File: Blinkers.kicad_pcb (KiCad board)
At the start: 2 copper layers, 238 x 45 mm, 218 parts, among them J1 12V, J2 A1, J3 gnd, J4 A1, J5 A1, J6 A1, J7 A1, J8 A1, Q1 Q_NMOS_DGS, Q2 Q_NMOS_DGS, Q3 Q_NMOS_DGS, Q4 Q_NMOS_DGS, Q5 Q_NMOS_DGS, Q6 Q_NMOS_DGS

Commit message: Modified D_2835 to make it work with specifications for LEDs. Moved VDD and GND pins to appropriate locations near center of board.
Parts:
- D1, D10, D101, D102, D103, D104, D105, D106, D107, D108, D11, D110, D111, D112, D113, D114, D115, D116, D117, D118, D12, D120, D121, D122, D123, D124, D125, D126, D128, D129, D13, D130, D131, D132, D133, D134, D135, D137, D138, D139, D140, D141, D142, D143, D144, D145, D147, D148, D149, D15, D150, D151, D152, D153, D155, D156, D157, D158, D159, D16, D160, D161, D162, D164, D165, D166, D167, D168, D169, D17, D170, D171, D172, D174, D18, D19, D2, D20, D22, D24, D25, D27, D28, D29, D3, D30, D31, D32, D33, D34, D35, D36, D37, D38, D39, D4, D41, D42, D43, D44, D45, D46, D47, D48, D49, D5, D51, D52, D53, D54, D55, D56, D57, D58, D59, D6, D61, D62, D63, D64, D65, D66, D68, D69, D70, D71, D72, D73, D74, D75, D77, D78, D79, D8, D80, D81, D82, D83, D84, D85, D87, D88, D9, D90, D91, D93, D94, D95, D96, D97, D98, D99: footprint Footprints:D_2835_FLIPPED -> Footprints:D_2835
- moved J3 56.8 mm to (214.6, 119.4)
- moved J1 55.7 mm to (214.6, 104.1)

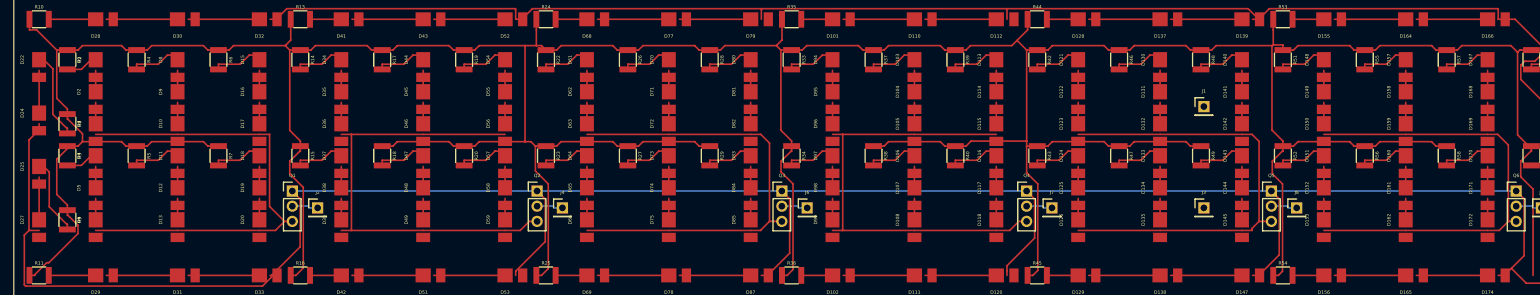
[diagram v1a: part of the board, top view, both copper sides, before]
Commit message: Changed positioning of LED grid with Array tool.
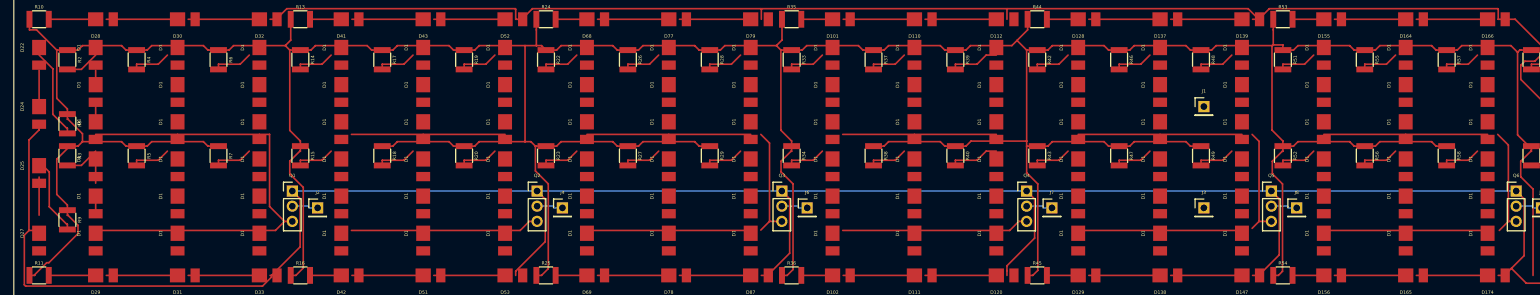
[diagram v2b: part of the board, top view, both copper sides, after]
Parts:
- removed D10, D103, D104, D105, D106, D107, D108, D11, D113, D114, D115, D116, D117, D118, D12, D121, D122, D123, D124, D125, D126, D13, D130, D131, D132, D133, D134, D135, D140, D141, D142, D143, D144, D145, D148, D149, D15, D150, D151, D152, D153, D157, D158, D159, D16, D160, D161, D162, D167, D168, D169, D17, D170, D171, D172, D18, D19, D2, D20, D3, D34, D35, D36, D37, D38, D39, D4, D44, D45, D46, D47, D48, D49, D5, D54, D55, D56, D57, D58, D59, D6, D61, D62, D63, D64, D65, D66, D70, D71, D72, D73, D74, D75, D8, D80, D81, D82, D83, D84, D85, D9, D94, D95, D96, D97, D98, D99: LED, Footprints:D_2835
- added D1: LED, Footprints:D_2835, F.Cu at (257.3, 123.2)
- added D1: LED, Footprints:D_2835, F.Cu at (146.4, 123.2)
- added D1: LED, Footprints:D_2835, F.Cu at (146.4, 95.2)
- added D1: LED, Footprints:D_2835, F.Cu at (134.1, 95.2)
- added D1: LED, Footprints:D_2835, F.Cu at (121.8, 95.2)
- added D1: LED, Footprints:D_2835, F.Cu at (109.5, 95.2)
- added D1: LED, Footprints:D_2835, F.Cu at (97.2, 95.2)
- added D1: LED, Footprints:D_2835, F.Cu at (84.8, 95.2)
- added D1: LED, Footprints:D_2835, F.Cu at (72.5, 95.2)
- added D1: LED, Footprints:D_2835, F.Cu at (60.2, 95.2)
- added D1: LED, Footprints:D_2835, F.Cu at (134.1, 123.2)
- added D1: LED, Footprints:D_2835, F.Cu at (121.8, 123.2)
- added D1: LED, Footprints:D_2835, F.Cu at (109.5, 123.2)
- added D1: LED, Footprints:D_2835, F.Cu at (97.2, 123.2)
- added D1: LED, Footprints:D_2835, F.Cu at (84.8, 123.2)
- added D1: LED, Footprints:D_2835, F.Cu at (72.5, 123.2)
- added D1: LED, Footprints:D_2835, F.Cu at (60.2, 123.2)
- added D1: LED, Footprints:D_2835, F.Cu at (47.9, 123.2)
- added D1: LED, Footprints:D_2835, F.Cu at (257.3, 117.6)
- added D1: LED, Footprints:D_2835, F.Cu at (245.0, 123.2)
- added D1: LED, Footprints:D_2835, F.Cu at (245.0, 117.6)
- added D1: LED, Footprints:D_2835, F.Cu at (232.7, 117.6)
- added D1: LED, Footprints:D_2835, F.Cu at (220.4, 117.6)
- added D1: LED, Footprints:D_2835, F.Cu at (208.0, 117.6)
- added D1: LED, Footprints:D_2835, F.Cu at (195.7, 117.6)
- added D1: LED, Footprints:D_2835, F.Cu at (183.4, 117.6)
- added D1: LED, Footprints:D_2835, F.Cu at (171.1, 117.6)
- added D1: LED, Footprints:D_2835, F.Cu at (158.8, 117.6)
- added D1: LED, Footprints:D_2835, F.Cu at (146.4, 117.6)
- added D1: LED, Footprints:D_2835, F.Cu at (134.1, 117.6)
- added D1: LED, Footprints:D_2835, F.Cu at (232.7, 123.2)
- added D1: LED, Footprints:D_2835, F.Cu at (121.8, 117.6)
- added D1: LED, Footprints:D_2835, F.Cu at (109.5, 117.6)
- added D1: LED, Footprints:D_2835, F.Cu at (97.2, 117.6)
- added D1: LED, Footprints:D_2835, F.Cu at (84.8, 117.6)
- added D1: LED, Footprints:D_2835, F.Cu at (72.5, 117.6)
- added D1: LED, Footprints:D_2835, F.Cu at (60.2, 117.6)
- added D1: LED, Footprints:D_2835, F.Cu at (47.9, 117.6)
- added D1: LED, Footprints:D_2835, F.Cu at (257.3, 112.0)
- added D1: LED, Footprints:D_2835, F.Cu at (245.0, 112.0)
- added D1: LED, Footprints:D_2835, F.Cu at (232.7, 112.0)
- added D1: LED, Footprints:D_2835, F.Cu at (220.4, 123.2)
- added D1: LED, Footprints:D_2835, F.Cu at (220.4, 112.0)
- added D1: LED, Footprints:D_2835, F.Cu at (208.0, 112.0)
- added D1: LED, Footprints:D_2835, F.Cu at (195.7, 112.0)
- added D1: LED, Footprints:D_2835, F.Cu at (183.4, 112.0)
- added D1: LED, Footprints:D_2835, F.Cu at (171.1, 112.0)
- added D1: LED, Footprints:D_2835, F.Cu at (158.8, 112.0)
- added D1: LED, Footprints:D_2835, F.Cu at (146.4, 112.0)
- added D1: LED, Footprints:D_2835, F.Cu at (134.1, 112.0)
- added D1: LED, Footprints:D_2835, F.Cu at (121.8, 112.0)
- added D1: LED, Footprints:D_2835, F.Cu at (109.5, 112.0)
- added D1: LED, Footprints:D_2835, F.Cu at (208.0, 123.2)
- added D1: LED, Footprints:D_2835, F.Cu at (97.2, 112.0)
- added D1: LED, Footprints:D_2835, F.Cu at (84.8, 112.0)
- added D1: LED, Footprints:D_2835, F.Cu at (72.5, 112.0)
- added D1: LED, Footprints:D_2835, F.Cu at (60.2, 112.0)
- added D1: LED, Footprints:D_2835, F.Cu at (47.9, 112.0)
- added D1: LED, Footprints:D_2835, F.Cu at (257.3, 106.4)
- added D1: LED, Footprints:D_2835, F.Cu at (245.0, 106.4)
- added D1: LED, Footprints:D_2835, F.Cu at (232.7, 106.4)
- added D1: LED, Footprints:D_2835, F.Cu at (220.4, 106.4)
- added D1: LED, Footprints:D_2835, F.Cu at (208.0, 106.4)
- added D1: LED, Footprints:D_2835, F.Cu at (195.7, 123.2)
- added D1: LED, Footprints:D_2835, F.Cu at (195.7, 106.4)
- added D1: LED, Footprints:D_2835, F.Cu at (183.4, 106.4)
- added D1: LED, Footprints:D_2835, F.Cu at (171.1, 106.4)
- added D1: LED, Footprints:D_2835, F.Cu at (158.8, 106.4)
- added D1: LED, Footprints:D_2835, F.Cu at (146.4, 106.4)
- added D1: LED, Footprints:D_2835, F.Cu at (134.1, 106.4)
- added D1: LED, Footprints:D_2835, F.Cu at (121.8, 106.4)
- added D1: LED, Footprints:D_2835, F.Cu at (109.5, 106.4)
- added D1: LED, Footprints:D_2835, F.Cu at (97.2, 106.4)
- added D1: LED, Footprints:D_2835, F.Cu at (84.8, 106.4)
- added D1: LED, Footprints:D_2835, F.Cu at (183.4, 123.2)
- added D1: LED, Footprints:D_2835, F.Cu at (72.5, 106.4)
- added D1: LED, Footprints:D_2835, F.Cu at (60.2, 106.4)
- added D1: LED, Footprints:D_2835, F.Cu at (47.9, 106.4)
- added D1: LED, Footprints:D_2835, F.Cu at (257.3, 100.8)
- added D1: LED, Footprints:D_2835, F.Cu at (245.0, 100.8)
- added D1: LED, Footprints:D_2835, F.Cu at (232.7, 100.8)
- added D1: LED, Footprints:D_2835, F.Cu at (220.4, 100.8)
- added D1: LED, Footprints:D_2835, F.Cu at (208.0, 100.8)
- added D1: LED, Footprints:D_2835, F.Cu at (195.7, 100.8)
- added D1: LED, Footprints:D_2835, F.Cu at (183.4, 100.8)
- added D1: LED, Footprints:D_2835, F.Cu at (171.1, 123.2)
- added D1: LED, Footprints:D_2835, F.Cu at (171.1, 100.8)
- added D1: LED, Footprints:D_2835, F.Cu at (158.8, 100.8)
- added D1: LED, Footprints:D_2835, F.Cu at (146.4, 100.8)
- added D1: LED, Footprints:D_2835, F.Cu at (134.1, 100.8)
- added D1: LED, Footprints:D_2835, F.Cu at (121.8, 100.8)
- added D1: LED, Footprints:D_2835, F.Cu at (109.5, 100.8)
- added D1: LED, Footprints:D_2835, F.Cu at (97.2, 100.8)
- added D1: LED, Footprints:D_2835, F.Cu at (84.8, 100.8)
- added D1: LED, Footprints:D_2835, F.Cu at (72.5, 100.8)
- added D1: LED, Footprints:D_2835, F.Cu at (60.2, 100.8)
- added D1: LED, Footprints:D_2835, F.Cu at (158.8, 123.2)
- added D1: LED, Footprints:D_2835, F.Cu at (47.9, 100.8)
- added D1: LED, Footprints:D_2835, F.Cu at (257.3, 95.2)
- added D1: LED, Footprints:D_2835, F.Cu at (245.0, 95.2)
- added D1: LED, Footprints:D_2835, F.Cu at (232.7, 95.2)
- added D1: LED, Footprints:D_2835, F.Cu at (220.4, 95.2)
- added D1: LED, Footprints:D_2835, F.Cu at (208.0, 95.2)
- added D1: LED, Footprints:D_2835, F.Cu at (195.7, 95.2)
- added D1: LED, Footprints:D_2835, F.Cu at (183.4, 95.2)
- added D1: LED, Footprints:D_2835, F.Cu at (171.1, 95.2)
- added D1: LED, Footprints:D_2835, F.Cu at (158.8, 95.2)
- moved D27 2.03 mm to (39.4, 123.2)
- moved D1 1.84 mm to (47.9, 95.2)
- moved D22 1.84 mm to (39.4, 95.2)
- moved D24 0.98 mm to (39.4, 104.1)
- moved D25 0.12 mm to (39.4, 113.0)
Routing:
- net Net-(D1-Pad1): track 2.52 -> 81.5 mm
- net Net-(D123-Pad1): track 69.5 -> 41.5 mm
- net Net-(D150-Pad1): track 69.4 -> 41.5 mm
- net Net-(D63-Pad1): track 69.7 -> 42.0 mm
- net Net-(D105-Pad1): track 68.9 -> 51.4 mm
- net Net-(D36-Pad1): track 69.1 -> 51.6 mm
- net GND: track 597.7 -> 603.4 mm
- net Net-(D22-Pad1): track 5.73 -> 0.00 mm
- net Net-(D25-Pad2): track 12.0 -> 17.7 mm
- net Net-(D25-Pad1): track 5.73 -> 0.00 mm
- net Net-(D65-Pad1): track 2.52 -> 0.00 mm
- net Net-(D97-Pad1): track 2.52 -> 0.00 mm
- net Net-(D94-Pad1): track 2.52 -> 0.00 mm
- net Net-(D98-Pad1): track 2.52 -> 0.00 mm
- net Net-(D83-Pad1): track 2.52 -> 0.00 mm
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
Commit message: Aligned right side of outer ring.
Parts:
- moved D93 2.03 mm to (270.5, 123.2)
- moved D88 1.84 mm to (270.5, 95.2)
- moved D25 0.85 mm to (39.4, 113.9)
- moved D90 0.55 mm to (270.5, 104.6)
- moved D24 0.43 mm to (39.4, 104.6)
- moved D91 0.17 mm to (270.5, 113.3)
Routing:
- net GND: track 603.4 -> 609.1 mm
- net Net-(D88-Pad1): track 5.73 -> 0.00 mm
- net Net-(D91-Pad2): track 6.82 -> 12.5 mm
- net Net-(D91-Pad1): track 5.73 -> 0.00 mm
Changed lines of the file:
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@@
-(kicad_pcb (version 20171130) (host pcbnew "(5.1.2)-2")
+(kicad_pcb (version 20171130) (host pcbnew 5.1.2-f72e74a~84~ubuntu18.04.1)
   (general
     (thickness 1.6)
@@
   )
   (module Footprints:D_2835 locked placed (layer F.Cu)
-    (at 39.37 104.14 270)
+    (at 39.37 104.567 270)
     (fp_text reference D24 (at 0 2.54 270) (layer F.SilkS)
       (effects (font (size 0.5 0.5) (thickness 0.0625)))
@@
   )
   (module Footprints:D_2835 locked placed (layer F.Cu)
-    (at 39.37 113.03 270)
+    (at 39.37 113.883 270)
     (fp_text reference D25 (at 0 2.54 270) (layer F.SilkS)
       (effects (font (size 0.5 0.5) (thickness 0.0625)))
@@
   )
   (module Footprints:D_2835 placed (layer F.Cu)
-    (at 270.51 97.0875 270)
+    (at 270.51 95.25 270)
     (fp_text reference D88 (at 0 2.54 270) (layer F.SilkS)
       (effects (font (size 0.5 0.5) (thickness 0.0625)))
@@
   )
   (module Footprints:D_2835 placed (layer F.Cu)
-    (at 270.51 105.117 270)
+    (at 270.51 104.567 270)
     (fp_text reference D90 (at 0 2.54 270) (layer F.SilkS)
       (effects (font (size 0.5 0.5) (thickness 0.0625)))
@@
   )
   (module Footprints:D_2835 placed (layer F.Cu)
-    (at 270.51 113.146 270)
+    (at 270.51 113.3167 270)
     (fp_text reference D91 (at 0 2.54 270) (layer F.SilkS)
       (effects (font (size 0.5 0.5) (thickness 0.0625)))
@@
   )
   (module Footprints:D_2835 placed (layer F.Cu)
-    (at 270.51 121.175 270)
+    (at 270.51 123.2 270)
     (fp_text reference D93 (at 0 2.54 270) (layer F.SilkS)
       (effects (font (size 0.5 0.5) (thickness 0.0625)))
@@
   (gr_line (start 35.56 87.63) (end 35.56 132.63) (angle 90) (layer Edge.Cuts) (width 0.15))
   (segment (start 47.88 98.6875) (end 47.88 101.205) (width 0.25) (layer F.Cu) (net 1))
+  (segment (start 47.88 103.505) (end 47.88 106.022) (width 0.25) (layer F.Cu) (net 1))
+  (segment (start 47.88 117.958) (end 47.88 120.475) (width 0.25) (layer F.Cu) (net 1))
+  (segment (start 134.12 122.775) (end 121.8 122.775) (width 0.25) (layer F.Cu) (net 1))
+  (segment (start 146.44 122.775) (end 134.12 122.775) (width 0.25) (layer F.Cu) (net 1))
+  (segment (start 208.04 122.775) (end 195.72 122.775) (width 0.25) (layer F.Cu) (net 1))
+  (segment (start 220.36 122.775) (end 208.04 122.775) (width 0.25) (layer F.Cu) (net 1))
+  (segment (start 245 122.775) (end 232.68 122.775) (width 0.25) (layer F.Cu) (net 1))
+  (segment (start 257.32 122.775) (end 245 122.775) (width 0.25) (layer F.Cu) (net 1))
   (segment (start 47.88 96.3875) (end 45.73 98.5375) (width 0.25) (layer F.Cu) (net 2))
   (segment (start 45.73 98.5375) (end 43.625 98.5375) (width 0.25) (layer F.Cu) (net 2))
-  (segment (start 47.88 103.505) (end 47.88 106.022) (width 0.25) (layer F.Cu) (net 1))
+  (segment (start 47.88 113.14) (end 47.88 115.658) (width 0.25) (layer F.Cu) (net 2))
   (segment (start 72.52 108.322) (end 74.0453 108.322) (width 0.25) (layer F.Cu) (net 3))
   (segment (start 74.0453 108.322) (end 74.0453 119.1626) (width 0.25) (layer F.Cu) (net 3))
@@
   (segment (start 60.2 122.775) (end 72.52 122.775) (width 0.25) (layer F.Cu) (net 3))
   (segment (start 47.88 122.775) (end 60.2 122.775) (width 0.25) (layer F.Cu) (net 3))
-  (segment (start 47.88 113.14) (end 47.88 115.658) (width 0.25) (layer F.Cu) (net 2))
   (segment (start 47.88 110.84) (end 45.73 112.99) (width 0.25) (layer F.Cu) (net 4))
   (segment (start 45.73 112.99) (end 43.625 112.99) (width 0.25) (layer F.Cu) (net 4))
-  (segment (start 47.88 117.958) (end 47.88 120.475) (width 0.25) (layer F.Cu) (net 1))
   (segment (start 54.04 98.5375) (end 54.04 97.7622) (width 0.25) (layer F.Cu) (net 5))
   (segment (start 58.6747 96.3875) (end 57.3 97.7622) (width 0.25) (layer F.Cu) (net 5))
@@
   (segment (start 111.08 129.54) (end 111.08 128.9075) (width 0.25) (layer F.Cu) (net 9))
   (segment (start 270.51 106.717) (end 268.9847 106.717) (width 0.25) (layer F.Cu) (net 9))
+  (segment (start 39.37 104.417) (end 39.37 98.6875) (width 0.25) (layer F.Cu) (net 9))
   (segment (start 177.24 110.09) (end 178.8353 110.09) (width 0.25) (layer F.Cu) (net 10))
   (segment (start 187.9647 109.331) (end 179.5943 109.331) (width 0.25) (layer F.Cu) (net 10))
@@
   (segment (start 77.47 119.126) (end 79.8507 119.126) (width 0.25) (layer B.Cu) (net 11))
   (segment (start 79.8507 119.126) (end 80.1047 119.38) (width 0.25) (layer B.Cu) (net 11))
-  (segment (start 39.37 104.417) (end 39.37 98.6875) (width 0.25) (layer F.Cu) (net 9))
   (segment (start 43.625 108.172) (end 43.625 107.3967) (width 0.25) (layer F.Cu) (net 13))
   (segment (start 39.37 96.3875) (end 41.4381 98.4556) (width 0.25) (layer F.Cu) (net 13))
@@
   (segment (start 134.12 108.322) (end 121.8 108.322) (width 0.25) (layer F.Cu) (net 36))
   (segment (start 146.44 108.322) (end 134.12 108.322) (width 0.25) (layer F.Cu) (net 36))
-  (segment (start 134.12 122.775) (end 121.8 122.775) (width 0.25) (layer F.Cu) (net 1))
-  (segment (start 146.44 122.775) (end 134.12 122.775) (width 0.25) (layer F.Cu) (net 1))
   (segment (start 151.13 121.412) (end 149.9547 121.412) (width 0.25) (layer F.Cu) (net 36))
   (segment (start 115.64 112.99) (end 115.64 112.2147) (width 0.25) (layer F.Cu) (net 37))
@@
   (segment (start 144.9147 110.84) (end 143.54 112.2147) (width 0.25) (layer F.Cu) (net 47))
   (segment (start 143.54 112.2147) (end 140.28 112.2147) (width 0.25) (layer F.Cu) (net 47))
-  (segment (start 270.51 104.417) (end 270.51 98.6875) (width 0.25) (layer F.Cu) (net 48))
+  (segment (start 270.51 104.417) (end 270.51 98.6875) (width 0.25) (layer F.Cu) (net 9))
   (segment (start 270.51 96.3875) (end 268.9847 96.3875) (width 0.25) (layer F.Cu) (net 49))
   (segment (start 263.915 98.5375) (end 263.915 97.7622) (width 0.25) (layer F.Cu) (net 49))
   (segment (start 268.9847 96.3875) (end 267.61 97.7622) (width 0.25) (layer F.Cu) (net 49))
   (segment (start 267.61 97.7622) (end 263.915 97.7622) (width 0.25) (layer F.Cu) (net 49))
-  (segment (start 270.51 120.475) (end 270.51 114.746) (width 0.25) (layer F.Cu) (net 50))
+  (segment (start 270.51 120.475) (end 270.51 114.746) (width 0.25) (layer F.Cu) (net 51))
   (segment (start 263.915 112.99) (end 265.5103 112.99) (width 0.25) (layer F.Cu) (net 51))
   (segment (start 270.51 112.446) (end 266.0543 112.446) (width 0.25) (layer F.Cu) (net 51))
@@
   (segment (start 194.1947 96.3875) (end 192.82 97.7622) (width 0.25) (layer F.Cu) (net 67))
   (segment (start 192.82 97.7622) (end 189.56 97.7622) (width 0.25) (layer F.Cu) (net 67))
-  (segment (start 208.04 122.775) (end 195.72 122.775) (width 0.25) (layer F.Cu) (net 1))
-  (segment (start 220.36 122.775) (end 208.04 122.775) (width 0.25) (layer F.Cu) (net 1))
   (segment (start 222.9332 121.412) (end 222.9332 109.3699) (width 0.25) (layer F.Cu) (net 68))
   (segment (start 222.9332 109.3699) (end 221.8853 108.322) (width 0.25) (layer F.Cu) (net 68))
@@
   (segment (start 245 108.322) (end 232.68 108.322) (width 0.25) (layer F.Cu) (net 81))
   (segment (start 257.32 108.322) (end 245 108.322) (width 0.25) (layer F.Cu) (net 81))
-  (segment (start 245 122.775) (end 232.68 122.775) (width 0.25) (layer F.Cu) (net 1))
-  (segment (start 257.32 122.775) (end 245 122.775) (width 0.25) (layer F.Cu) (net 1))
   (segment (start 226.52 112.99) (end 226.52 112.2147) (width 0.25) (layer F.Cu) (net 82))
   (segment (start 231.1547 110.84) (end 229.78 112.2147) (width 0.25) (layer F.Cu) (net 82))
